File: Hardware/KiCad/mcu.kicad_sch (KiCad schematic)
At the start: 9 parts, among them U3 STM32F427ZGTx, Y1 8 MHz, Y2 32 kHz

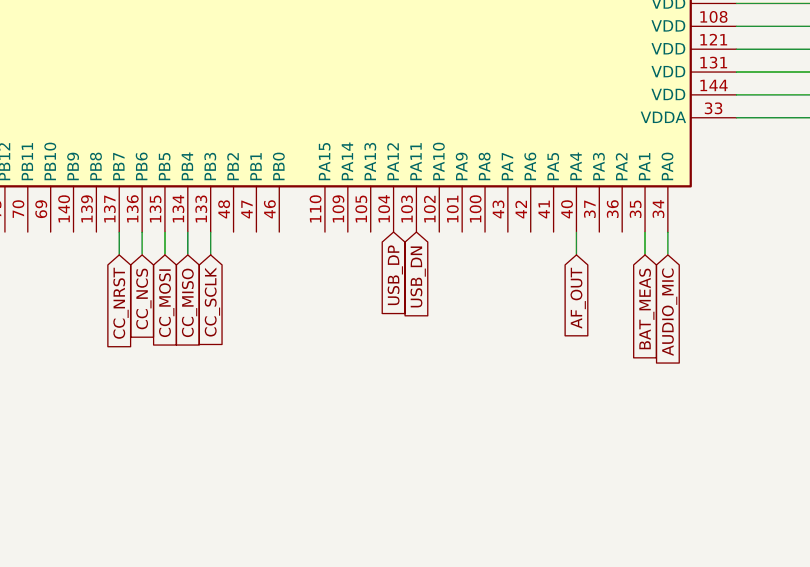
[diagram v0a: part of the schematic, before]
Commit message: Use standard notation for USB lines and fix label types
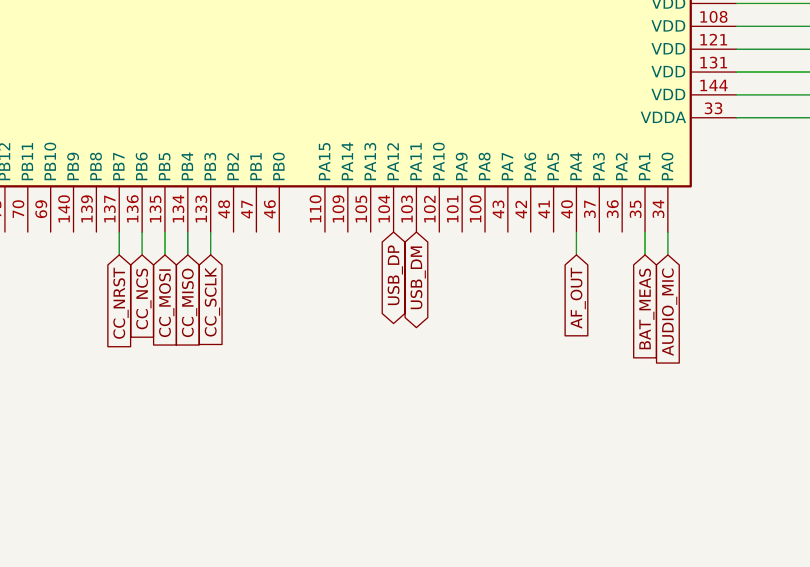
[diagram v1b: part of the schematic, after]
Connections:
- net USB_DN renamed USB_DM
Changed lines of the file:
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@@
     )
   )
-  (global_label "USB_DP" (shape input) (at 208.28 132.08 270) (fields_autoplaced)
+  (global_label "USB_DP" (shape bidirectional) (at 208.28 132.08 270) (fields_autoplaced)
     (effects (font (size 1.27 1.27)) (justify right))
     (property "Intersheet References" "${INTERSHEET_REFS}" (id 0) (at 208.2006 141.8107 90)
@@
     )
   )
-  (global_label "USB_DN" (shape input) (at 210.82 132.08 270) (fields_autoplaced)
-    (effects (font (size 1.27 1.27)) (justify right))
-    (property "Intersheet References" "${INTERSHEET_REFS}" (id 0) (at 210.7406 141.8712 90)
-      (effects (font (size 1.27 1.27)) (justify right) hide)
-    )
+  (global_label "USB_DM" (shape bidirectional) (at 210.82 132.08 270) (fields_autoplaced)
+    (effects (font (size 1.27 1.27)) (justify right))
+    (property "Intersheet References" "${INTERSHEET_REFS}" (id 0) (at 210.7406 141.9921 90)
+      (effects (font (size 1.27 1.27)) (justify right) hide)
+    )

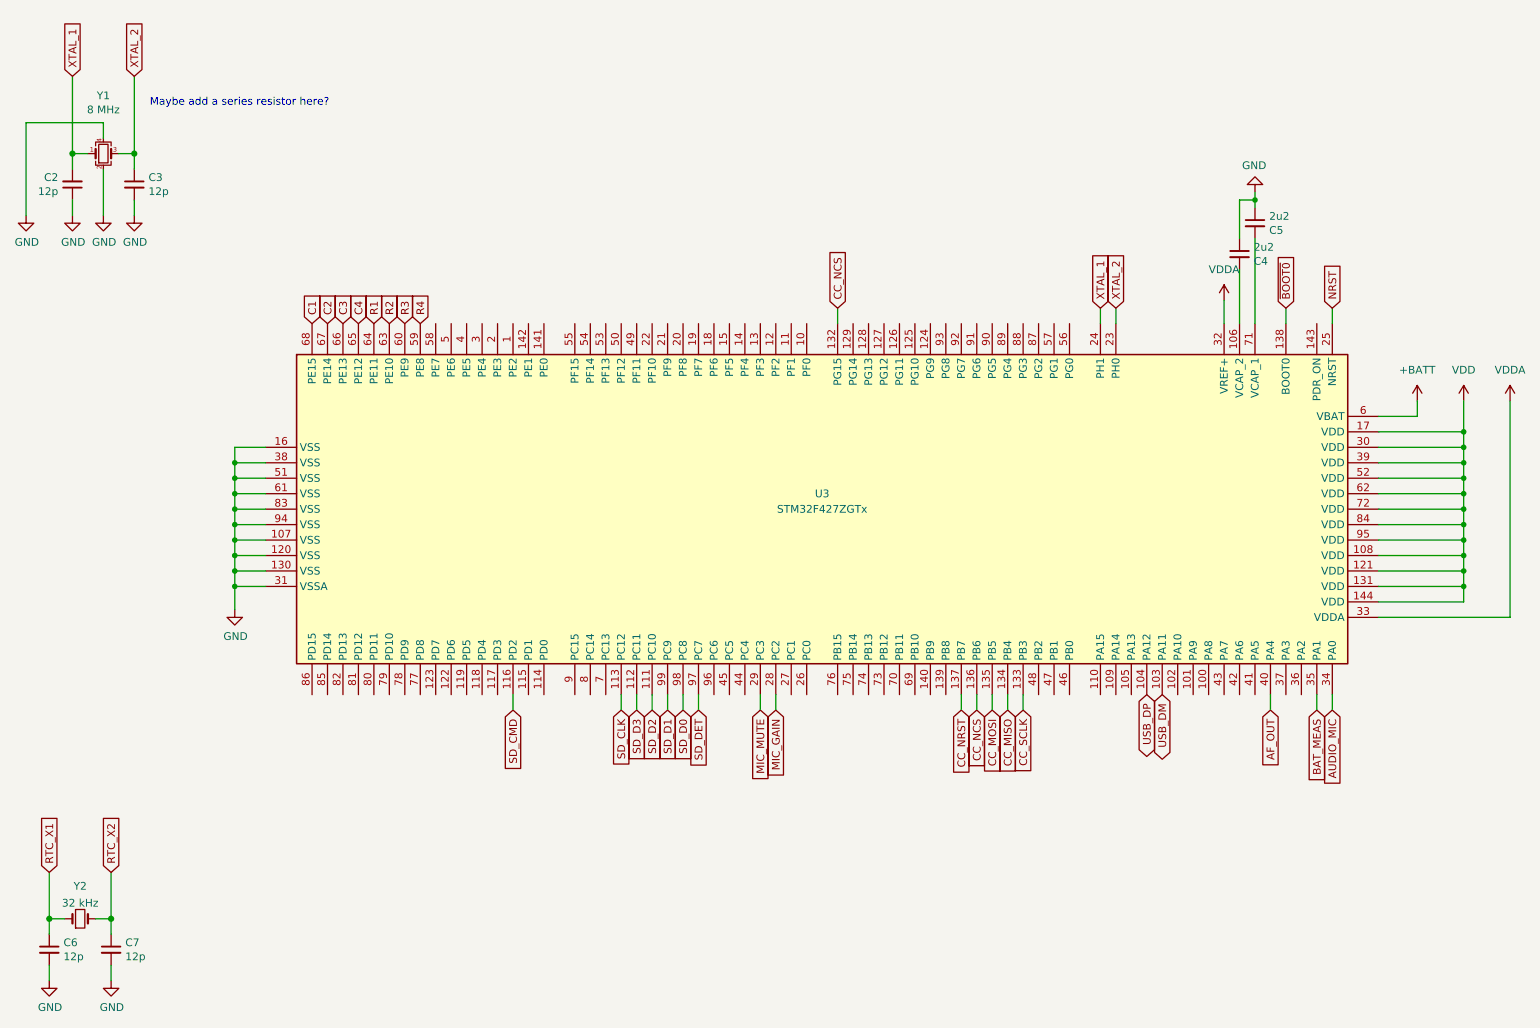
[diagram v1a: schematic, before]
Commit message: Add no connection labels, anotate schematic, regen pdf and create netlist
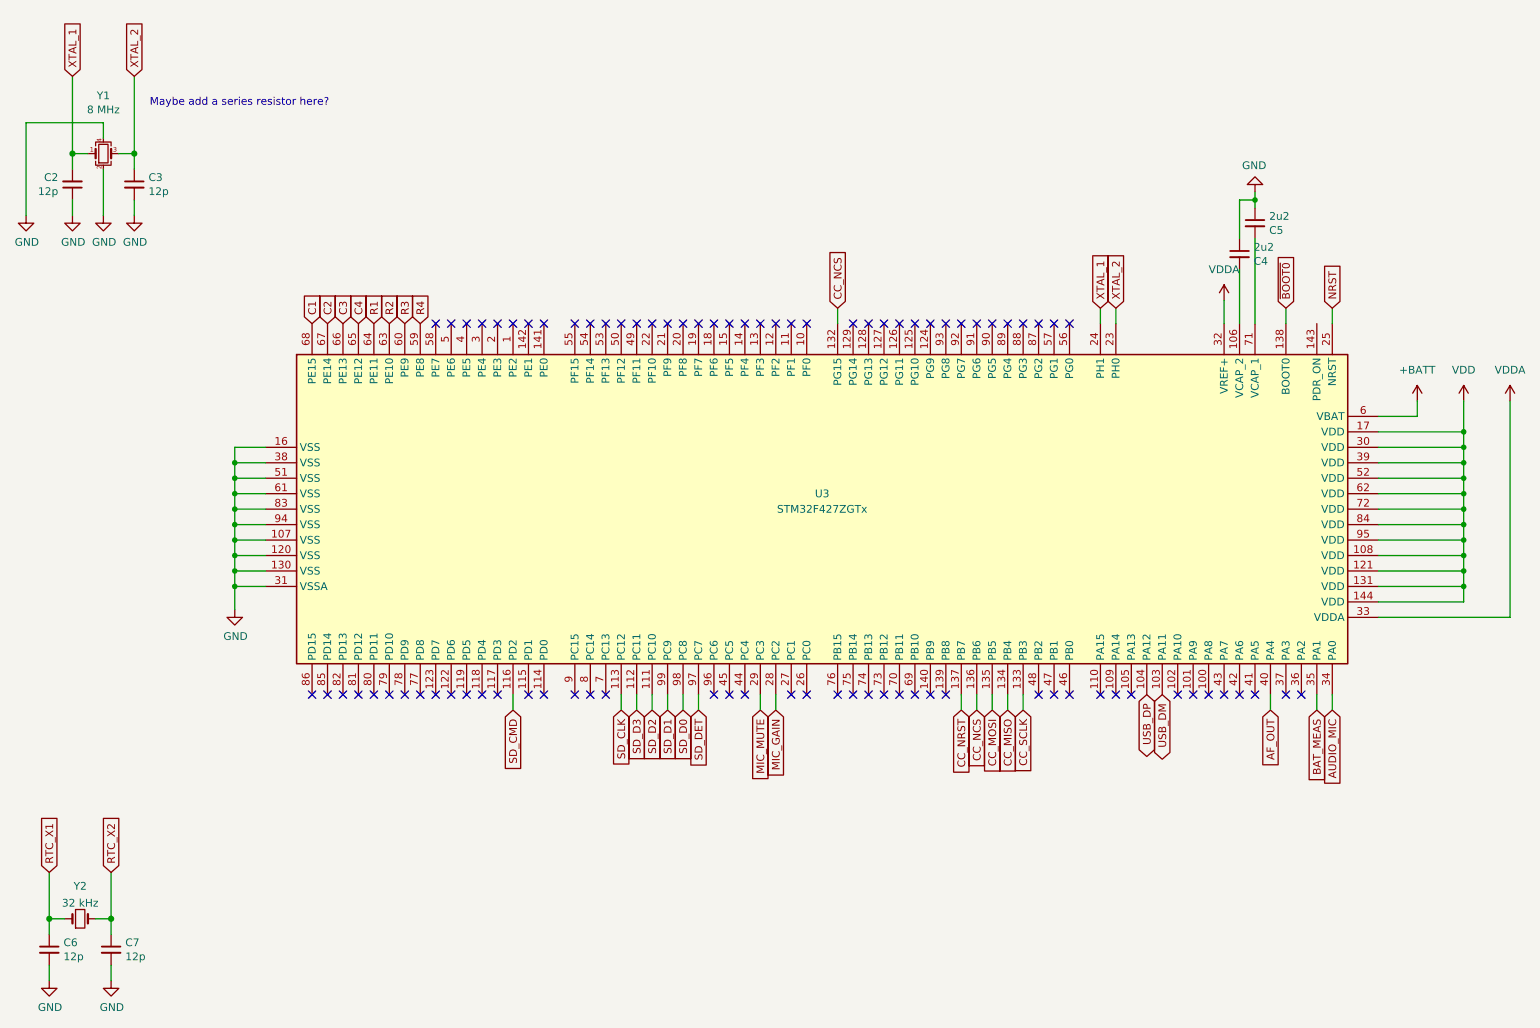
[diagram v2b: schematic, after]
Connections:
- no-connect marks 0 -> 84
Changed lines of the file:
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@@
   (junction (at 260.35 109.22) (diameter 0) (color 0 0 0 0)
   )
+  (no_connect (at 119.38 132.08))
+  (no_connect (at 101.6 132.08))
+  (no_connect (at 99.06 132.08))
+  (no_connect (at 96.52 132.08))
+  (no_connect (at 93.98 132.08))
+  (no_connect (at 91.44 132.08))
+  (no_connect (at 114.3 71.12))
+  (no_connect (at 116.84 71.12))
+  (no_connect (at 119.38 71.12))
+  (no_connect (at 121.92 71.12))
+  (no_connect (at 116.84 132.08))
+  (no_connect (at 114.3 132.08))
+  (no_connect (at 109.22 132.08))
+  (no_connect (at 106.68 132.08))
+  (no_connect (at 88.9 132.08))
+  (no_connect (at 86.36 132.08))
+  (no_connect (at 83.82 132.08))
+  (no_connect (at 81.28 132.08))
+  (no_connect (at 78.74 132.08))
+  (no_connect (at 76.2 132.08))
+  (no_connect (at 73.66 132.08))
+  (no_connect (at 71.12 132.08))
+  (no_connect (at 106.68 71.12))
+  (no_connect (at 109.22 71.12))
+  (no_connect (at 129.54 71.12))
+  (no_connect (at 132.08 71.12))
+  (no_connect (at 91.44 71.12))
+  (no_connect (at 93.98 71.12))
+  (no_connect (at 96.52 71.12))
+  (no_connect (at 99.06 71.12))
+  (no_connect (at 101.6 71.12))
+  (no_connect (at 104.14 71.12))
+  (no_connect (at 124.46 71.12))
+  (no_connect (at 127 71.12))
+  (no_connect (at 233.68 132.08))
+  (no_connect (at 231.14 132.08))
+  (no_connect (at 215.9 132.08))
+  (no_connect (at 213.36 132.08))
+  (no_connect (at 226.06 132.08))
+  (no_connect (at 223.52 132.08))
+  (no_connect (at 220.98 132.08))
+  (no_connect (at 218.44 132.08))
+  (no_connect (at 142.24 71.12))
+  (no_connect (at 144.78 71.12))
+  (no_connect (at 147.32 71.12))
+  (no_connect (at 142.24 132.08))
+  (no_connect (at 139.7 132.08))
+  (no_connect (at 137.16 132.08))
+  (no_connect (at 134.62 71.12))
+  (no_connect (at 137.16 71.12))
+  (no_connect (at 139.7 71.12))
+  (no_connect (at 160.02 71.12))
+  (no_connect (at 162.56 71.12))
+  (no_connect (at 149.86 71.12))
+  (no_connect (at 152.4 71.12))
+  (no_connect (at 165.1 71.12))
+  (no_connect (at 167.64 71.12))
+  (no_connect (at 170.18 71.12))
+  (no_connect (at 172.72 71.12))
+  (no_connect (at 175.26 71.12))
+  (no_connect (at 177.8 71.12))
+  (no_connect (at 180.34 71.12))
+  (no_connect (at 182.88 71.12))
+  (no_connect (at 185.42 71.12))
+  (no_connect (at 187.96 71.12))
+  (no_connect (at 190.5 71.12))
+  (no_connect (at 193.04 71.12))
+  (no_connect (at 195.58 71.12))
+  (no_connect (at 165.1 132.08))
+  (no_connect (at 162.56 132.08))
+  (no_connect (at 160.02 132.08))
+  (no_connect (at 157.48 132.08))
+  (no_connect (at 152.4 132.08))
+  (no_connect (at 149.86 132.08))
+  (no_connect (at 205.74 132.08))
+  (no_connect (at 203.2 132.08))
+  (no_connect (at 200.66 132.08))
+  (no_connect (at 195.58 132.08))
+  (no_connect (at 193.04 132.08))
+  (no_connect (at 190.5 132.08))
+  (no_connect (at 175.26 132.08))
+  (no_connect (at 172.72 132.08))
+  (no_connect (at 170.18 132.08))
+  (no_connect (at 167.64 132.08))
   (wire (pts (xy 58.42 118.11) (xy 58.42 114.3))
     (stroke (width 0) (type default) (color 0 0 0 0))
